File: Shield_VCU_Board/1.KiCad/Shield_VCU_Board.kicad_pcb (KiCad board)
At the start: 2 copper layers, 250.5 x 107.1 mm, 159 parts, among them J1 Conn_02x08_Odd_Even, J10 Main_Supply, J11 Conn_01x40_Socket, J13 Conn_Molex_TouchPanel, J14 CAN_OUT, J15 Conn_01x04_Socket, J16 CAN_IN, J2 Conn_02x10_Odd_Even, J3/1 NXP3, J4 Conn_02x08_Odd_Even, J5 Conn_02x10_Odd_Even, J6 Conn_02x10_Odd_Even, J7 Button_Activation_Logic, J8 Conn_ToSpeaker, Q1 BSS138, Q2 BSS138, Q3 BSS138, Q4 BSS138, U1 AS1115-BSST, U10 TPS61165-Q1, U13 TPS54202DDC, U2 SN74LVC1G125DBV, U3 MC74HC14A, U4 TPA6211A1 - ?, U7 FT813Q, U8 TLV76133DCY, U9 TLV76133DCY

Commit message: Updated resistors for audio
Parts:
- R12, R14: value 10k1% -> 300R1%
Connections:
- 5V3 pad 1: +5.3V -> +5V
- C31 pad 1: +5.3V -> +5V
- C33 pad 1: +5.3V -> +5V
- D10 pad 1: +5.3V -> +5V
- D9 pad 1: +5.3V -> +5V
- JP1 pad 2: +5.3V -> +5V
- U8 pad 3: +5.3V -> +5V
- U9 pad 3: +5.3V -> +5V
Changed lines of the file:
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@@
 			)
 		)
-		(property "Value" "10k1%"
+		(property "Value" "300R1%"
 			(at 0 -1.829999 90)
 			(layer "B.Fab")
@@
 			(layers "B.Cu" "B.Mask" "B.Paste")
 			(roundrect_rratio 0.25)
-			(net "+5.3V")
+			(net "+5V")
 			(pinfunction "VI_3")
 			(pintype "power_in")
@@
 			(layers "B.Cu" "B.Mask" "B.Paste")
 			(roundrect_rratio 0.25)
-			(net "+5.3V")
+			(net "+5V")
 			(pinfunction "K_1")
 			(pintype "passive")
@@
 			(size 1 1)
 			(layers "B.Cu" "B.Mask")
-			(net "+5.3V")
+			(net "+5V")
 			(pinfunction "1_1")
 			(pintype "passive")
@@
 			(layers "B.Cu" "B.Mask" "B.Paste")
 			(roundrect_rratio 0.25)
-			(net "+5.3V")
+			(net "+5V")
 			(pinfunction "VI_3")
 			(pintype "power_in")
@@
 			)
 		)
-		(property "Value" "10k1%"
+		(property "Value" "300R1%"
 			(at 0 -1.829999 90)
 			(layer "B.Fab")
@@
 			(layers "B.Cu" "B.Mask" "B.Paste")
 			(roundrect_rratio 0.212766)
-			(net "+5.3V")
+			(net "+5V")
 			(pintype "passive")
 		)
@@
 			(size 1 0.5)
 			(layers "B.Cu" "B.Mask")
-			(net "+5.3V")
+			(net "+5V")
 			(pinfunction "B_2")
 			(pintype "passive")
@@
 			(layers "B.Cu" "B.Mask" "B.Paste")
 			(roundrect_rratio 0.212766)
-			(net "+5.3V")
+			(net "+5V")
 			(pintype "passive")
 		)
@@
 			)
 		)
-		(attr smd)
+		(attr smd dnp)
 		(duplicate_pad_numbers_are_jumpers no)
 		(fp_line
@@
 			)
 		)
-		(attr smd)
+		(attr smd dnp)
 		(duplicate_pad_numbers_are_jumpers no)
 		(fp_line
@@
 			(layers "B.Cu" "B.Mask" "B.Paste")
 			(roundrect_rratio 0.25)
-			(net "+5.3V")
+			(net "+5V")
 			(pinfunction "K_1")
 			(pintype "passive")
@@
 	)
 	(group ""
-		(members "c25f9d26-0d31-49c8-ab0f-2cbe13a2767e")
-	)
-	(group ""

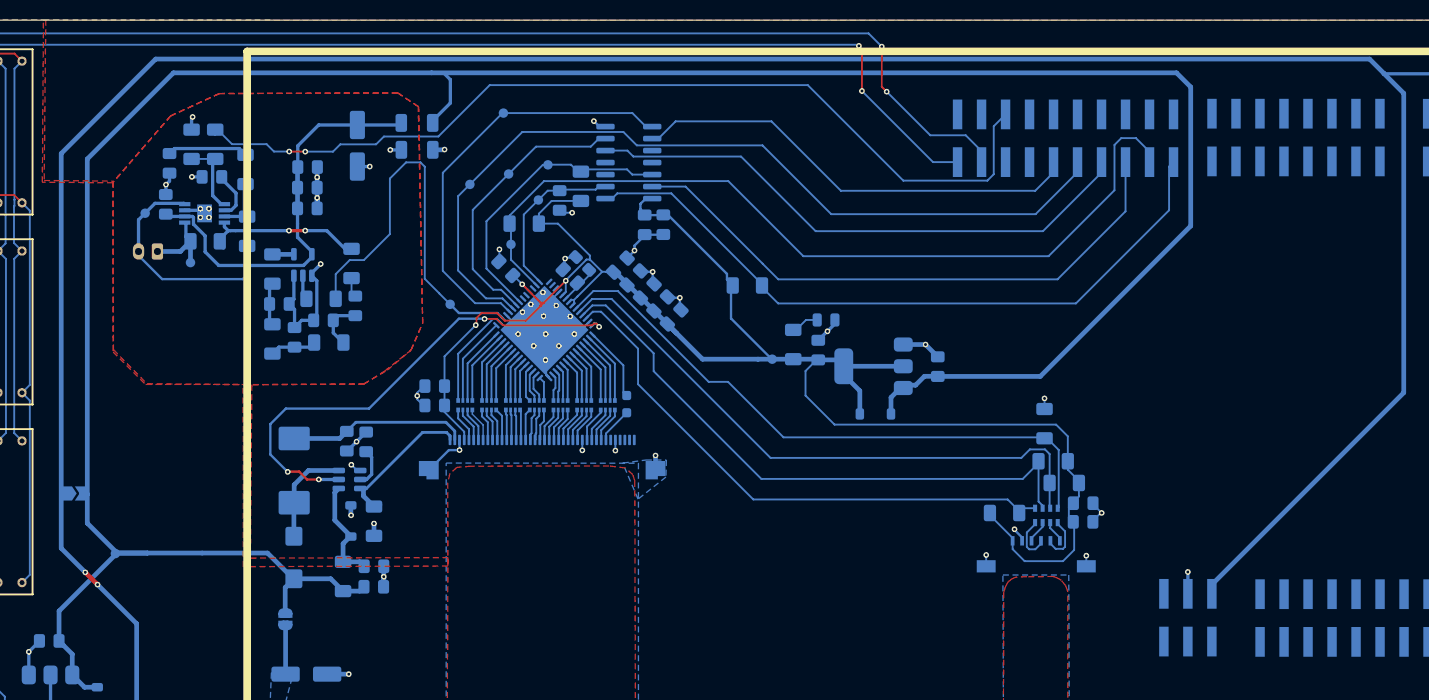
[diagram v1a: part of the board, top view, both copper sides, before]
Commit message: Corrections on TouchScreen pin RST & INT swap
*Additional: 33R resistor footprint change to match real part
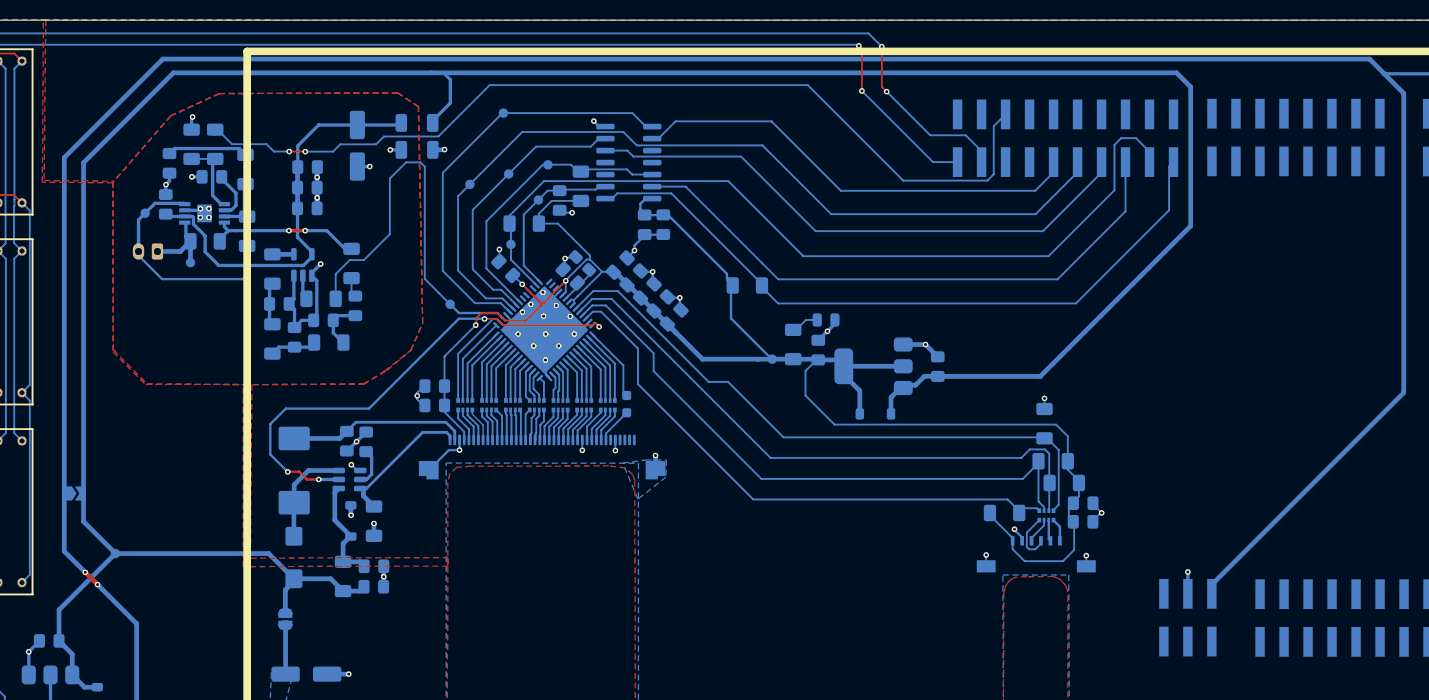
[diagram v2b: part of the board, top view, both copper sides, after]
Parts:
- RN8: footprint Resistor_SMD:R_Cat16-4 -> Resistor_SMD:R_Array_Convex_4x0402
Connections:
- C38 pad 1: +5.3V -> +5V
- FB2 pad 1: +5.3V -> +5V
- JP3 pad 2: +5.3V -> +5V
- L2 pad 1: +5.3V -> +5V
- R19 pad 2: +5.3V -> +5V
- RN8 pad 1: Net-(J13-Pin_5) -> Net-(J13-Pin_6)
- RN8 pad 2: Net-(J13-Pin_6) -> Net-(J13-Pin_5)
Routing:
- net +5.3V: track 283.3 -> 0.00 mm
- net +5V: track 0.00 -> 279.0 mm
- net Net-(J13-Pin_5): track 5.08 -> 2.26 mm
- net BAT+: track 429.6 -> 428.9 mm
